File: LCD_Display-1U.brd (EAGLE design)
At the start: 50.8 x 25.4 mm, 4 parts, among them U1 NEWHAVEN_LCD

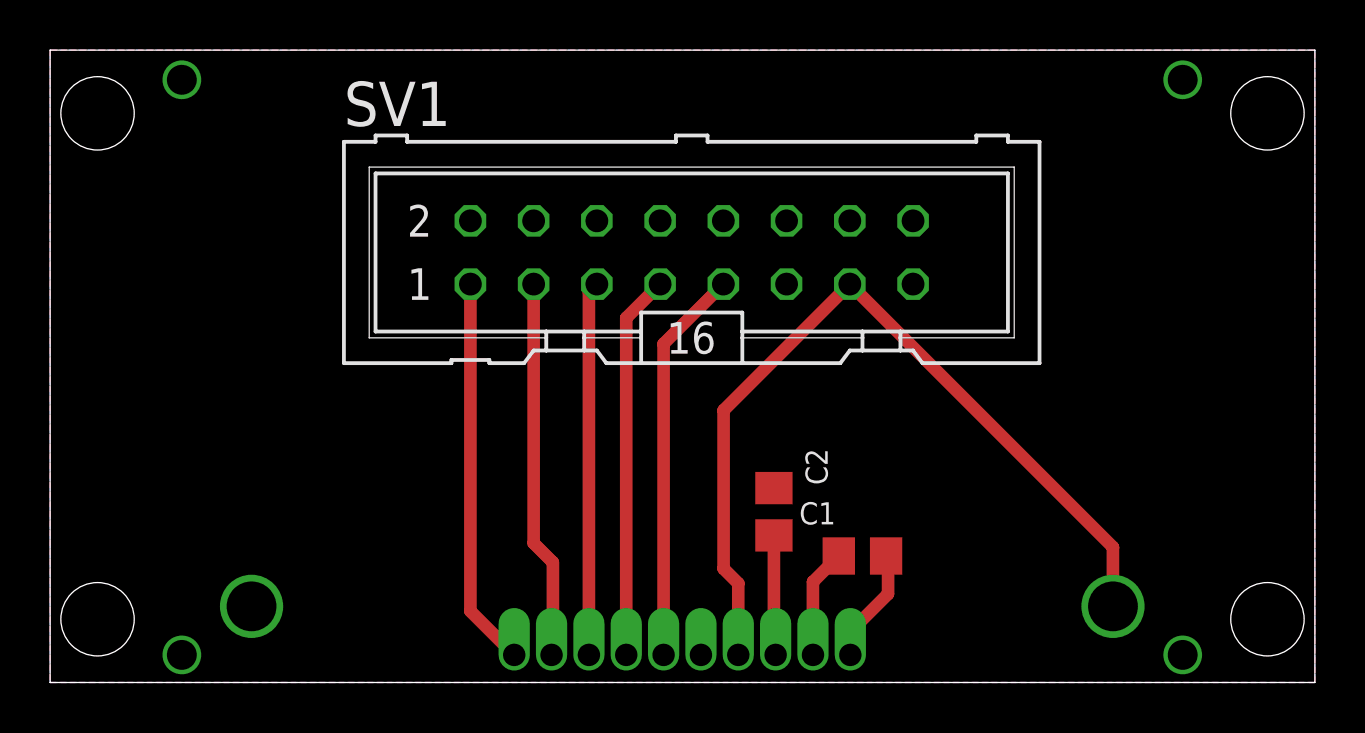
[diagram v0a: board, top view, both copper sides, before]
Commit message: Re-routed several mcu-accessory boards to be (mostly) single-layer
Will make printing easier on LKPF machine.
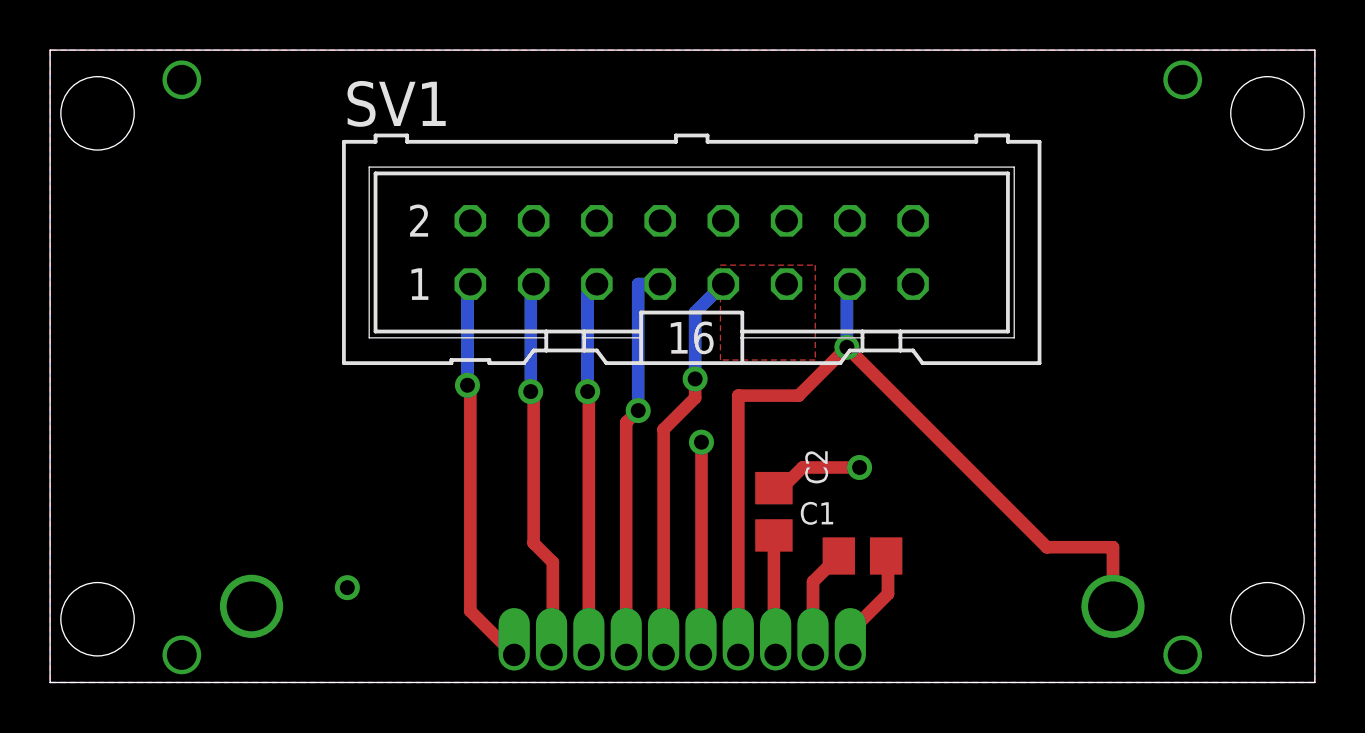
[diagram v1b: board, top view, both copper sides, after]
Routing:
- net GND: track 0.00 -> 12.3 mm, vias 0 -> 3
- net SCL: track 15.5 -> 16.0 mm, vias 0 -> 1
- net RST: track 15.6 -> 15.7 mm, vias 0 -> 1
- net RS: track 15.2 -> 15.3 mm, vias 0 -> 1
- net CSB: track 15.0 -> 15.1 mm, vias 0 -> 1
- net VDD: vias 0 -> 1
- net SI: vias 0 -> 1
- added copper zone on layer 1, net N$4
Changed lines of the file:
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@@
 <setting verticaltext="up"/>
 </settings>
-<grid distance="0.025" unitdist="inch" unit="inch" style="lines" multiple="1" display="yes" altdistance="0.025" altunitdist="inch" altunit="inch"/>
+<grid distance="0.01" unitdist="inch" unit="inch" style="lines" multiple="1" display="yes" altdistance="0.025" altunitdist="inch" altunit="inch"/>
 <layers>
 <layer number="1" name="Top" color="4" fill="1" visible="yes" active="yes"/>
@@
 <contactref element="U1" pad="K"/>
 <contactref element="SV1" pad="11"/>
-<polygon width="0.508" layer="1" isolate="0.381">
+<polygon width="0.508" layer="1" isolate="1.27" thermals="no">
 <vertex x="0" y="0"/>
 <vertex x="50.8" y="0"/>
@@
 <vertex x="0" y="25.4"/>
 </polygon>
-<polygon width="0.508" layer="16" isolate="0.381">
+<polygon width="0.508" layer="16" isolate="1.27" thermals="no">
 <vertex x="0" y="25.4"/>
 <vertex x="50.8" y="25.4"/>
@@
 <vertex x="0" y="0"/>
 </polygon>
+<wire x1="26.141" y1="1.108" x2="26.162" y2="1.129" width="0.508" layer="1"/>
+<wire x1="26.162" y1="1.129" x2="26.162" y2="9.652" width="0.508" layer="1"/>
+<via x="26.162" y="9.652" extent="1-16" drill="0.6" shape="square"/>
+<via x="32.512" y="8.636" extent="1-16" drill="0.6" shape="square"/>
+<wire x1="29.073" y1="7.808" x2="29.398" y2="7.808" width="0.508" layer="1"/>
+<wire x1="29.398" y1="7.808" x2="30.226" y2="8.636" width="0.508" layer="1"/>
+<wire x1="30.226" y1="8.636" x2="32.512" y2="8.636" width="0.508" layer="1"/>
+<via x="11.938" y="3.81" extent="1-16" drill="0.6" shape="square"/>
 </signal>
 <signal name="VDD">
@@
 <contactref element="U1" pad="7"/>
 <contactref element="SV1" pad="13"/>
-<wire x1="27.051" y1="10.932" x2="32.121" y2="16.002" width="0.508" layer="1"/>
-<wire x1="27.641" y1="1.108" x2="27.641" y2="3.982" width="0.508" layer="1"/>
-<wire x1="27.641" y1="3.982" x2="27.051" y2="4.572" width="0.508" layer="1"/>
-<wire x1="27.051" y1="4.572" x2="27.051" y2="10.932" width="0.508" layer="1"/>
 <wire x1="42.691" y1="3.058" x2="42.691" y2="5.432" width="0.508" layer="1"/>
-<wire x1="42.691" y1="5.432" x2="32.121" y2="16.002" width="0.508" layer="1"/>
+<wire x1="27.641" y1="1.108" x2="27.641" y2="11.522" width="0.508" layer="1"/>
+<wire x1="27.641" y1="11.522" x2="30.064" y2="11.522" width="0.508" layer="1"/>
+<wire x1="30.064" y1="11.522" x2="32.004" y2="13.462" width="0.508" layer="1"/>
+<via x="32.004" y="13.462" extent="1-16" drill="0.6" shape="square"/>
+<wire x1="32.004" y1="13.462" x2="32.004" y2="15.885" width="0.508" layer="16"/>
+<wire x1="32.004" y1="15.885" x2="32.121" y2="16.002" width="0.508" layer="16"/>
+<wire x1="42.691" y1="5.432" x2="40.034" y2="5.432" width="0.508" layer="1"/>
+<wire x1="40.034" y1="5.432" x2="32.004" y2="13.462" width="0.508" layer="1"/>
 </signal>
 <signal name="SI">
 <contactref element="U1" pad="5"/>
 <contactref element="SV1" pad="9"/>
-<wire x1="24.641" y1="1.108" x2="24.641" y2="13.602" width="0.508" layer="1"/>
-<wire x1="24.641" y1="13.602" x2="27.041" y2="16.002" width="0.508" layer="1"/>
+<wire x1="24.641" y1="1.108" x2="24.641" y2="10.163" width="0.508" layer="1"/>
+<wire x1="24.641" y1="10.163" x2="25.908" y2="11.43" width="0.508" layer="1"/>
+<wire x1="25.908" y1="11.43" x2="25.908" y2="12.192" width="0.508" layer="1"/>
+<via x="25.908" y="12.192" extent="1-16" drill="0.6" shape="square"/>
+<wire x1="25.908" y1="12.192" x2="25.908" y2="14.869" width="0.508" layer="16"/>
+<wire x1="25.908" y1="14.869" x2="27.041" y2="16.002" width="0.508" layer="16"/>
 </signal>
 <signal name="SCL">
 <contactref element="U1" pad="4"/>
 <contactref element="SV1" pad="7"/>
-<wire x1="23.141" y1="1.108" x2="23.141" y2="14.642" width="0.508" layer="1"/>
-<wire x1="23.141" y1="14.642" x2="24.501" y2="16.002" width="0.508" layer="1"/>
+<wire x1="23.141" y1="1.108" x2="23.141" y2="10.441" width="0.508" layer="1"/>
+<wire x1="23.141" y1="10.441" x2="23.622" y2="10.922" width="0.508" layer="1"/>
+<via x="23.622" y="10.922" extent="1-16" drill="0.6" shape="square"/>
+<wire x1="23.622" y1="10.922" x2="23.622" y2="16.002" width="0.508" layer="16"/>
+<wire x1="23.622" y1="16.002" x2="24.501" y2="16.002" width="0.508" layer="16"/>
 </signal>
 <signal name="CSB">
 <contactref element="U1" pad="3"/>
 <contactref element="SV1" pad="5"/>
-<wire x1="21.641" y1="1.108" x2="21.641" y2="15.682" width="0.508" layer="1"/>
-<wire x1="21.641" y1="15.682" x2="21.961" y2="16.002" width="0.508" layer="1"/>
+<wire x1="21.641" y1="1.108" x2="21.641" y2="11.633" width="0.508" layer="1"/>
+<wire x1="21.641" y1="11.633" x2="21.59" y2="11.684" width="0.508" layer="1"/>
+<via x="21.59" y="11.684" extent="1-16" drill="0.6" shape="square"/>
+<wire x1="21.59" y1="11.684" x2="21.59" y2="15.631" width="0.508" layer="16"/>
+<wire x1="21.59" y1="15.631" x2="21.961" y2="16.002" width="0.508" layer="16"/>
 </signal>
 <signal name="RS">
 <contactref element="U1" pad="2"/>
 <contactref element="SV1" pad="3"/>
-<wire x1="19.421" y1="16.002" x2="19.421" y2="5.598" width="0.508" layer="1"/>
 <wire x1="19.421" y1="5.598" x2="20.193" y2="4.826" width="0.508" layer="1"/>
 <wire x1="20.193" y1="4.826" x2="20.193" y2="1.16" width="0.508" layer="1"/>
 <wire x1="20.193" y1="1.16" x2="20.141" y2="1.108" width="0.508" layer="1"/>
+<wire x1="19.421" y1="5.598" x2="19.421" y2="11.567" width="0.508" layer="1"/>
+<wire x1="19.421" y1="11.567" x2="19.304" y2="11.684" width="0.508" layer="1"/>
+<via x="19.304" y="11.684" extent="1-16" drill="0.6" shape="square"/>
+<wire x1="19.304" y1="11.684" x2="19.304" y2="15.885" width="0.508" layer="16"/>
+<wire x1="19.304" y1="15.885" x2="19.421" y2="16.002" width="0.508" layer="16"/>
 </signal>
 <signal name="RST">
 <contactref element="U1" pad="1"/>
 <contactref element="SV1" pad="1"/>
-<wire x1="16.881" y1="16.002" x2="16.881" y2="2.868" width="0.508" layer="1"/>
 <wire x1="16.881" y1="2.868" x2="18.641" y2="1.108" width="0.508" layer="1"/>
+<wire x1="16.881" y1="2.868" x2="16.881" y2="11.821" width="0.508" layer="1"/>
+<wire x1="16.881" y1="11.821" x2="16.764" y2="11.938" width="0.508" layer="1"/>
+<via x="16.764" y="11.938" extent="1-16" drill="0.6" shape="square"/>
+<wire x1="16.764" y1="11.938" x2="16.764" y2="15.885" width="0.508" layer="16"/>
+<wire x1="16.764" y1="15.885" x2="16.881" y2="16.002" width="0.508" layer="16"/>
+</signal>
+<signal name="N$4">
+<polygon width="0.254" layer="1" pour="cutout">
+<vertex x="26.924" y="16.764"/>
+<vertex x="30.734" y="16.764"/>
+<vertex x="30.734" y="12.954"/>
+<vertex x="26.924" y="12.954"/>
+</polygon>
 </signal>
 </signals>

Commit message: Modified LCD-1U for production run; added 8 pin ribbon connector
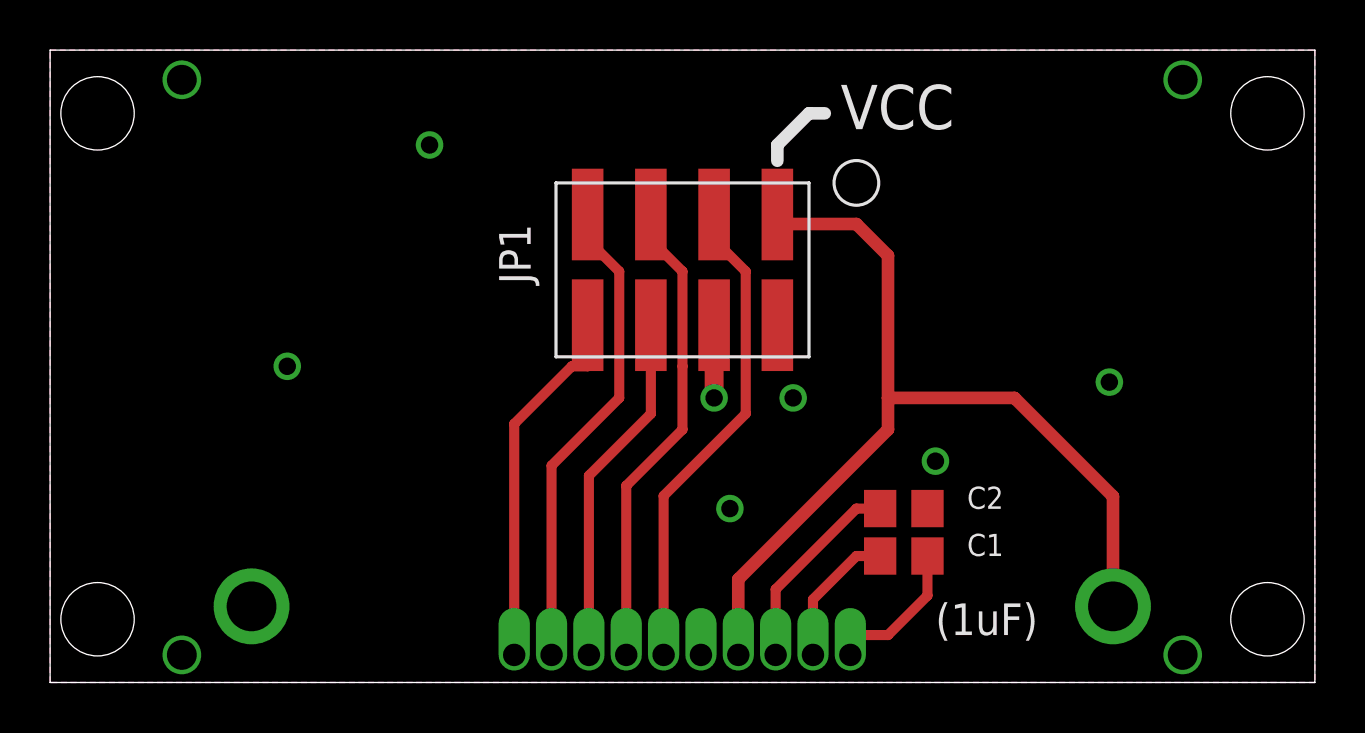
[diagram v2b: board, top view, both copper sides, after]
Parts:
- removed SV1: Ribbon Header, mcu-accessories:ML16
- added JP1: (no value), mcu-accessories:2X4SMT
- moved C2 5.22 mm to (34.3, 6.99), turned to 180 degrees
- moved C1 1.66 mm to (34.3, 5.08)
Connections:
- net CSB: now also JP1.6; no longer SV1.5
- net GND: now also JP1.2, JP1.4; no longer SV1.11
- net RS: now also JP1.7; no longer SV1.3
- net RST: now also JP1.8; no longer SV1.1
- net SCL: now also JP1.5; no longer SV1.7
- net SI: now also JP1.3; no longer SV1.9
- net VDD: now also JP1.1; no longer SV1.13
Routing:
- net GND: track 12.3 -> 2.92 mm, vias 3 -> 7
- net VDD: track 34.6 -> 38.7 mm, vias 1 -> 0
- net RS: track 15.3 -> 19.3 mm, vias 1 -> 0
- net SI: track 15.9 -> 19.6 mm, vias 1 -> 0
- net N$3: track 4.83 -> 8.18 mm
- net SCL: track 16.0 -> 19.1 mm, vias 1 -> 0
- net N$1: track 4.40 -> 5.97 mm
- net N$2: track 4.63 -> 6.00 mm
- net RST: track 15.7 -> 14.8 mm, vias 1 -> 0
- net CSB: track 15.1 -> 14.3 mm, vias 1 -> 0
- removed copper zone on layer 1, net N$4
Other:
- board text added: "(1uF)"
- board text added: "VCC"

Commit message: Fixed up Eurocard LCD module for production run
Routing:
- net GND: track 2.92 -> 8.85 mm
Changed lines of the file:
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@@
 <setting verticaltext="up"/>
 </settings>
-<grid distance="0.025" unitdist="inch" unit="inch" style="lines" multiple="1" display="yes" altdistance="0.025" altunitdist="inch" altunit="inch"/>
+<grid distance="0.001" unitdist="inch" unit="inch" style="lines" multiple="1" display="yes" altdistance="0.025" altunitdist="inch" altunit="inch"/>
 <layers>
 <layer number="1" name="Top" color="4" fill="1" visible="yes" active="yes"/>
@@
 <via x="15.24" y="21.59" extent="1-16" drill="0.7"/>
 <via x="27.305" y="6.985" extent="1-16" drill="0.7"/>
-<wire x1="26.67" y1="14.351" x2="26.67" y2="11.43" width="0.762" layer="1"/>
+<wire x1="26.67" y1="14.351" x2="26.67" y2="11.43" width="1.016" layer="1"/>
+<wire x1="27.305" y1="6.985" x2="27.305" y2="5.9182" width="1.016" layer="1"/>
+<wire x1="27.305" y1="5.9182" x2="26.1112" y2="4.7244" width="1.016" layer="1"/>
+<wire x1="26.1112" y1="4.7244" x2="26.1112" y2="1.6256" width="1.016" layer="1"/>
+<wire x1="26.1112" y1="1.6256" x2="26.162" y2="1.5748" width="1.016" layer="1"/>
 </signal>
 <signal name="VDD">
